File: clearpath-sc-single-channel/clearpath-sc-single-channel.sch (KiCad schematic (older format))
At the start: 56 parts, among them P1 MOLEX_MICROFIT_JR_RH_2x1_WAY, P2 MOLEX_MICROFIT_JR_RH_2x2_WAY, P3 MOLEX_MICROFIT_JR_RH_2x2_WAY, P4 MOLEX_MICROFIT_JR_RH_2x4_WAY, Q1 MMBT5401, Q2 MMBTA06, U1 LM317LCPK, U2 FT230XS-R, U3 USBLC6, U4 LM317LCPK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

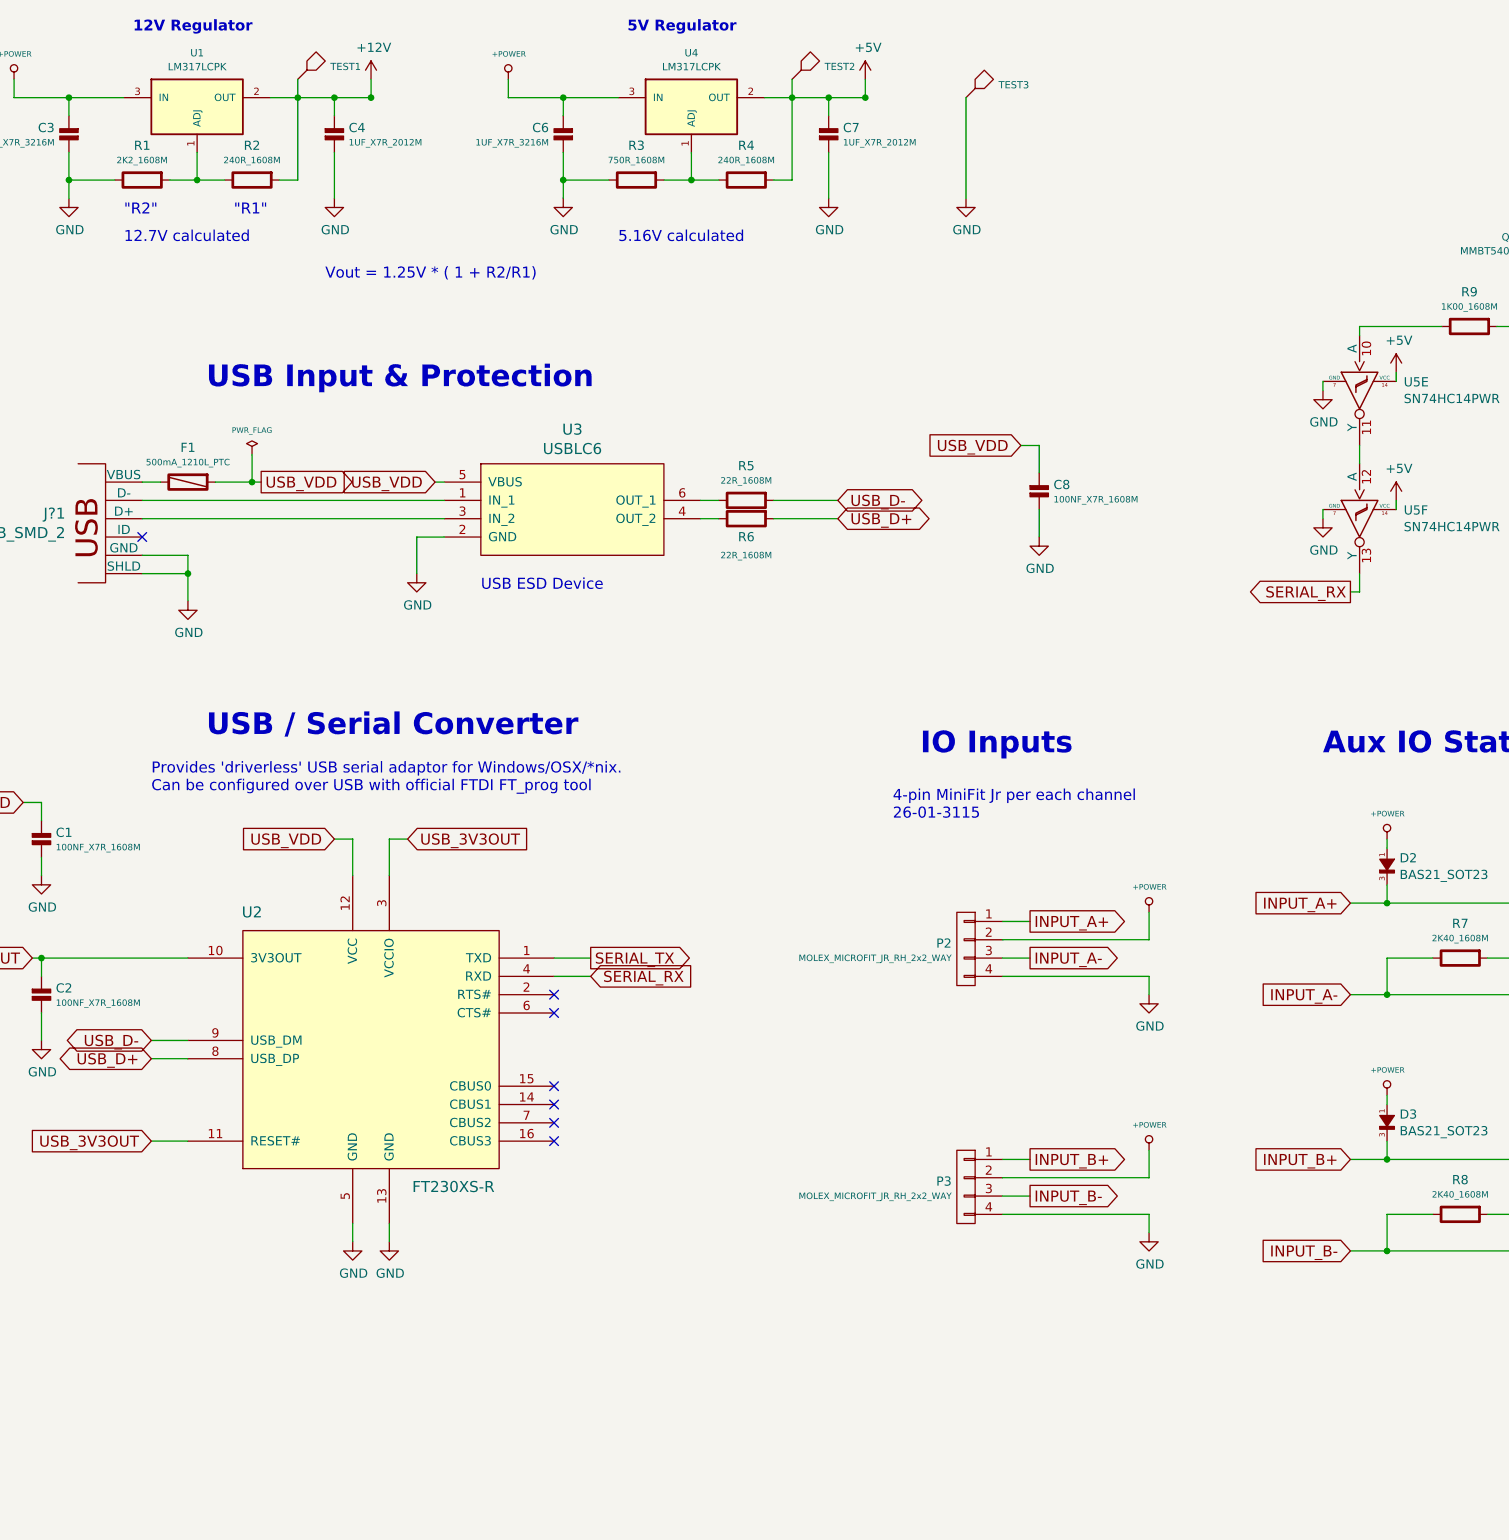
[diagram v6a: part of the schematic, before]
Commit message: Added aux connector, silkscreen labels and some final touches.
Ready for final check (pinout against SC4) and fab outputs
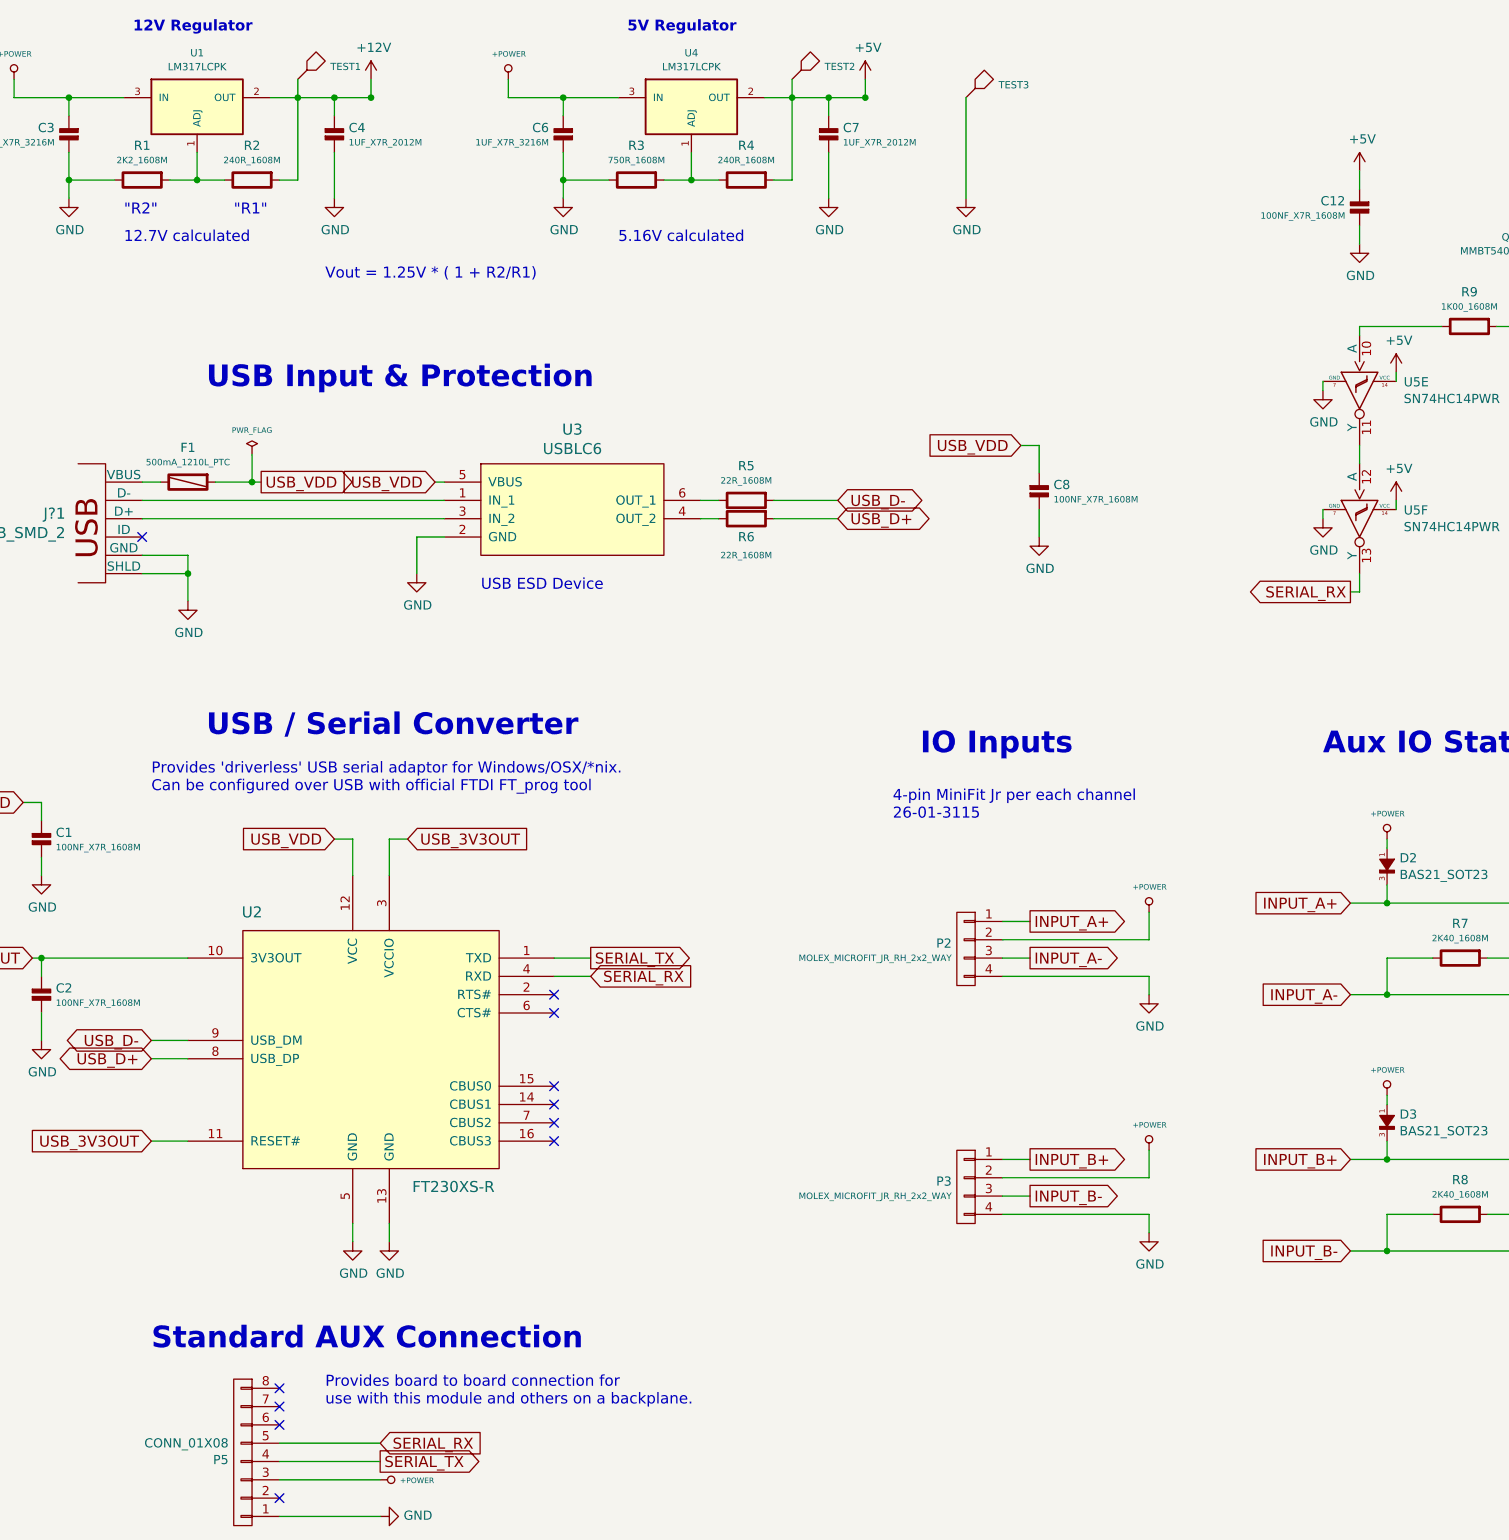
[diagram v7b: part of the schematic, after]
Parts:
- added C12: 100NF_X7R_1608M, Applidyne_Capacitor:CAPC1608X90N, symbol 100NF_X7R_1608M
- added P5: CONN_01X08, Applidyne_Connector_Wurth:61300811121, symbol CONN_01X08
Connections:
- net +5V: now also C12.1
- net +POWER: now also P5.3 (P3)
- net GND: now also C12.2, P5.1 (P1)
- net SERIAL_RX: now also P5.5 (P5)
- net SERIAL_TX: now also P5.4 (P4)
- no-connect marks 7 -> 11
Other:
- note added: "Provides board to board connection for \nuse with this module and others on a backplane."
- note added: "Standard AUX Connection"
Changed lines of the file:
@@
 LIBS:appli_linear
 LIBS:appli_link
+LIBS:appli_logic_devices
 LIBS:appli_logo
 LIBS:appli_memory
@@
 	1    0    0    -1
 $EndComp
+Wire Wire Line
+	2700 10900 3250 10900
+Wire Wire Line
+	2700 10700 3250 10700
+Wire Wire Line
+	2700 10600 3250 10600
+Wire Wire Line
+	2700 10500 3250 10500
+$Comp
+L GND #PWR050
+U 1 1 59CC5C46
+P 3250 10900
+F 0 "#PWR050" H 3250 10650 50  0001 C CNN
+F 1 "GND" V 3255 10772 50  0000 R CNN
+F 2 "" H 3250 10900 60  0000 C CNN
+F 3 "" H 3250 10900 60  0000 C CNN
+	1    3250 10900
+	0    -1   -1   0
+$EndComp
+$Comp
+L +POWER #PWR049
+U 1 1 59CC5DD0
+P 3250 10700
+F 0 "#PWR049" H 3250 10650 20  0001 C CNN
+F 1 "+POWER" V 3254 10808 30  0000 L CNN
+F 2 "" H 3250 10700 60  0000 C CNN
+F 3 "" H 3250 10700 60  0000 C CNN
+	1    3250 10700
+	0    1    1    0
+$EndComp
+Text GLabel 3250 10500 2    60   Input ~ 0
+SERIAL_RX
+Text GLabel 3250 10600 2    60   Output ~ 0
+SERIAL_TX
+$Comp
+L CONN_01X08 P5
+U 1 1 59CC67D2
+P 2500 10550
+F 0 "P5" H 2578 10591 50  0000 L CNN
+F 1 "CONN_01X08" H 2578 10500 50  0000 L CNN
+F 2 "Applidyne_Connector_Wurth:61300811121" V 2675 10550 50  0001 C CNN
+F 3 "http://www.farnell.com/cad/2124416.pdf" V 2750 10550 50  0001 C CNN
+F 4 "WURTH" H 2500 10100 60  0001 C CNN "manf"
+F 5 "61300811121" H 2500 10000 60  0001 C CNN "manf#"
+F 6 "Element 14" H 2500 9900 60  0001 C CNN "Supplier"
+F 7 "2356160" H 2500 9825 60  0001 C CNN "Supplier Part No"
+F 8 "http://au.element14.com/wurth-elektronik/61300811121/header-2-54mm-pin-tht-vertical/dp/2356160" H 2500 9725 60  0001 C CNN "Supplier URL"
+F 9 "0.358" H 2500 9625 60  0001 C CNN "Supplier Price"
+F 10 "1" H 2500 9525 60  0001 C CNN "Supplier Price Break"
+	1    2500 10550
+	-1   0    0    1
+$EndComp
+NoConn ~ 2700 10800
+NoConn ~ 2700 10400
+NoConn ~ 2700 10300
+NoConn ~ 2700 10200
+Text Notes 2000 10000 0    118  ~ 24
+Standard AUX Connection
+Text Notes 2950 10300 0    60   ~ 0
+Provides board to board connection for \nuse with this module and others on a backplane.
+$Comp
+L +5V #PWR051
+U 1 1 59CC88B8
+P 8600 3550
+F 0 "#PWR051" H 8600 3400 50  0001 C CNN
+F 1 "+5V" H 8615 3723 50  0000 C CNN
+F 2 "" H 8600 3550 60  0000 C CNN
+F 3 "" H 8600 3550 60  0000 C CNN
+	1    8600 3550
+	1    0    0    -1
+$EndComp
+$Comp
+L GND #PWR052
+U 1 1 59CC893F
+P 8600 3950
+F 0 "#PWR052" H 8600 3700 50  0001 C CNN
+F 1 "GND" H 8605 3777 50  0000 C CNN
+F 2 "" H 8600 3950 60  0000 C CNN
+F 3 "" H 8600 3950 60  0000 C CNN
+	1    8600 3950
+	1    0    0    -1
+$EndComp
+$Comp
+L 100NF_X7R_1608M C12
+U 1 1 59CC8AC5
+P 8600 3650
+F 0 "C12" H 8678 3585 50  0000 L CNN
+F 1 "100NF_X7R_1608M" H 8678 3505 35  0000 L CNN
+F 2 "Applidyne_Capacitor:CAPC1608X90N" V 8715 3550 20  0001 C CNN
+F 3 "http://www.farnell.com/datasheets/1732728.pdf" V 8740 3550 20  0001 C CNN
+F 4 "KEMET" V 8790 3550 20  0001 C CNN "manf"
+F 5 "C0603C104K5RACAUTO" V 8815 3550 20  0001 C CNN "manf#"
+F 6 "Element14" V 8840 3550 20  0001 C CNN "Supplier"
+F 7 "2070398" V 8865 3550 20  0001 C CNN "Supplier Part No"
+F 8 "http://au.element14.com/kemet/c0603c104k5racauto/cap-mlcc-x7r-100nf-50v-0603/dp/2070398" V 8890 3550 20  0001 C CNN "Supplier URL"
+F 9 "0.011" V 8915 3550 20  0001 C CNN "Supplier Price"
+F 10 "1" V 8940 3550 20  0001 C CNN "Supplier Price Break"
+	1    8600 3650
+	-1   0    0    -1
+$EndComp
+Wire Wire Line
+	8600 3550 8600 3650
+Wire Wire Line
+	8600 3850 8600 3950
 $EndSCHEMATC
